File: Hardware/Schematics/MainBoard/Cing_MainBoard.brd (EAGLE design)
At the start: 100 x 100 mm, 174 parts, among them IC1 L293D, IC2 LM2576S, IC3 FT232RL, IC5 BME280, Q1 16mhz, Q2 BSS138, Q3 BSS138, Q4 BSS138, Q5 BSS138, Q6 NP2301AMR-G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

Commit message: 3D package upgrade
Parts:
- VERSION: value 3.1 -> 4.0
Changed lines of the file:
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@@
 </layers>
 <board>
-<fusionsync huburn="a.cGVyc29uYWw6dWUyOTc5YzVj" projecturn="a.cGVyc29uYWw6dWUyOTc5YzVjIzIwMTYxMDE1NDY4MTE5MjY" f3durn="urn:adsk.wipprod:dm.lineage:OxtLfXioRNGpEPjqi8H5ew" pcbguid="aab246c0-a25e-424b-8ec7-c8b2cc11dcb0" lastpulledtime="" lastsyncedchangeguid="ba3a4b8f-c2b4-ea65-9e96-2cd773722963"/>
+<fusionsync huburn="a.cGVyc29uYWw6dWUyOTc5YzVj" projecturn="a.cGVyc29uYWw6dWUyOTc5YzVjIzIwMTkwNjI1MjAwNjYyNTAx" f3durn="urn:adsk.wipprod:dm.lineage:F-kKAJn1SLWSqLFyv44BXQ" pcbguid="94010e1c-0bc5-45e6-b30e-e8625a835ba8" lastpulledtime="" lastsyncedchangeguid="c102dd65-50ae-9bd8-6df9-751ffc4031cd"/>
 <plain>
 <text x="17.145" y="28.448" size="1.778" layer="21">Header 2</text>
@@
 <attribute name="VALUE" x="39.5" y="39.5" size="1.27" layer="21" rot="R135" align="bottom-center"/>
 </element>
-<element name="U$20" library="Cing Library" library_urn="urn:adsk.eagle:library:10154637" package="BALL" package3d_urn="urn:adsk.eagle:package:10154728/1" override_package3d_urn="urn:adsk.eagle:package:11838365/3" override_package_urn="urn:adsk.eagle:footprint:10154687/1" value="BALL" x="45" y="0" smashed="yes"/>
+<element name="U$20" library="Cing Library" library_urn="urn:adsk.eagle:library:10154637" package="BALL" package3d_urn="urn:adsk.eagle:package:10154728/1" override_package3d_urn="urn:adsk.eagle:package:11838365/5" override_package_urn="urn:adsk.eagle:footprint:10154687/1" value="BALL" x="45" y="0" smashed="yes"/>
 <element name="LED5" library="Cing Library" library_urn="urn:adsk.eagle:library:10154637" package="WS2812B" package3d_urn="urn:adsk.eagle:package:10154742/1" override_package3d_urn="urn:adsk.eagle:package:11838153/2" override_package_urn="urn:adsk.eagle:footprint:10154705/1" value="WS2812B" x="-34.29" y="-34.29" smashed="yes" rot="R270"/>
 <element name="LED6" library="Cing Library" library_urn="urn:adsk.eagle:library:10154637" package="WS2812B" package3d_urn="urn:adsk.eagle:package:10154742/1" override_package3d_urn="urn:adsk.eagle:package:11838143/2" override_package_urn="urn:adsk.eagle:footprint:10154705/1" value="WS2812B" x="-34.29" y="34.29" smashed="yes" rot="R180"/>
@@
 <attribute name="NAME" x="15.813" y="-26.546" size="1.27" layer="21" rot="R90"/>
 </element>
-<element name="VERSION" library="Cing Library" library_urn="urn:adsk.eagle:library:10154637" package="VERSION" package3d_urn="urn:adsk.eagle:package:10154717/1" value="3.1" x="49.5" y="0" smashed="yes" rot="R90">
+<element name="VERSION" library="Cing Library" library_urn="urn:adsk.eagle:library:10154637" package="VERSION" package3d_urn="urn:adsk.eagle:package:10154717/1" value="4.0" x="49.5" y="0" smashed="yes" rot="R90">
 <attribute name="VALUE" x="46.5" y="6.84" size="2.54" layer="21" rot="R90" align="center"/>
 </element>
@@
 <attribute name="VALUE" x="3.942" y="-33.6" size="1.27" layer="28" rot="MR90"/>
 </element>
-<element name="U$15" library="diy-modules" package="COMPASS-HMC5883L" override_package3d_urn="urn:adsk.eagle:package:11838453/4" override_package_urn="urn:adsk.eagle:footprint:11838454/1" value="" x="24.2" y="40.3" smashed="yes" rot="MR90">
+<element name="U$15" library="diy-modules" package="COMPASS-HMC5883L" override_package3d_urn="urn:adsk.eagle:package:11838453/5" override_package_urn="urn:adsk.eagle:footprint:11838454/1" value="" x="24.2" y="40.3" smashed="yes" rot="MR90">
 <attribute name="VALUE" x="16.58" y="40.3" size="1.27" layer="28" rot="MR90" align="top-center"/>
 </element>

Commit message: commit
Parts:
- added C23: 47uf, rcl:153CLV-0505
- added C24: 100n, rcl:C1206
- C17: value (none) -> 47uf; device rcl:E3,5-8 -> rcl:153CLV-0505
- moved C17 6.52 mm to (-20.9, 30.0), turned to 270 degrees
- moved R3 0.30 mm to (-23.1, -29.5)
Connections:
- net GND: now also C23.-, C24.2
- net VCC_MOT: now also C23.+, C24.1
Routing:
- net GND: track 832.2 -> 849.9 mm
- net VCC_MOT: track 42.9 -> 54.6 mm
- net VCC_SERVO: track 415.3 -> 421.4 mm, vias 11 -> 12
- net MOT_A+: track 71.5 -> 73.0 mm
- net BAT+: track 315.7 -> 314.4 mm
- net N$1: track 100.0 -> 98.8 mm
- net N$44: track 35.0 -> 34.0 mm
- net ATMEGA_D-: track 107.7 -> 106.6 mm
- net N$8: track 22.6 -> 21.6 mm

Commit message: commit
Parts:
- added C25, C26: 100n, rcl:C1206
- IC1: value L293D -> L293D
- moved C13 1.98 mm to (38.3, 31.8), turned to 90 degrees
- moved SW1 1.60 mm to (-43.8, -32.7)
- moved C9 1.08 mm to (-40.5, 35.2)
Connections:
- net +3V3: now also C26.2; no longer LED10.2, LED11.2, LED4.2, LED5.1, LED6.1, LED7.1, LED8.1, LED9.2
- net BAT+: no longer U$23.5
- net BUTTON: now also C26.1
- net GND: now also C25.1
- net RESET: now also C25.2
- net VCC_SERVO: now also LED10.2, LED11.2, LED4.2, LED5.1, LED6.1, LED7.1, LED8.1, LED9.2, U$23.5
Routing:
- net VCC_SERVO: track 421.4 -> 521.4 mm, vias 12 -> 15
- net GND: track 849.9 -> 874.9 mm, vias 45 -> 46
- net +3V3: track 661.1 -> 644.9 mm, vias 39 -> 40
- net RESET: track 195.4 -> 209.7 mm
- net BUTTON: track 19.0 -> 24.0 mm
- net N$1: track 98.8 -> 95.3 mm
- net SDA: track 247.9 -> 245.0 mm
- net ATMEGA_D+: track 102.2 -> 105.0 mm
- net D-: track 25.7 -> 23.3 mm
- net N$24: track 15.6 -> 13.3 mm
- net BAT-: track 106.4 -> 108.7 mm
- net D+: track 21.7 -> 19.4 mm
- net MOT_B-: track 66.5 -> 64.4 mm
- net N$13: track 18.2 -> 16.1 mm
- net SCL: track 241.2 -> 239.5 mm
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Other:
- board text added: "I2C"
- board text added: "USB"
- board text removed: "BT"

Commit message: commit
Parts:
- added U$10: MT3608SOT23-6, MT3608:SOT23-6
- moved R46 3.05 mm to (-13.0, 20.2), turned to 90 degrees
- moved R9 1.39 mm to (-15.2, 20.2), turned to 270 degrees
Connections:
- removed net N$44: D3.A, L1.2, U$5.P$1
- new net N$67: D3.A, L1.2, U$10.P$1, U$5.P$1
- net BAT+: now also U$10.P$4, U$10.P$5
- net GND: now also U$10.P$2
- net N$35: now also U$10.P$3
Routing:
- net N$67: track 0.00 -> 48.6 mm, vias 0 -> 2
- net N$44: track 34.0 -> 0.00 mm
- net N$46: track 33.7 -> 38.9 mm
- net N$35: track 15.5 -> 20.3 mm
- net BAT+: track 315.6 -> 319.6 mm
- net GND: track 874.9 -> 877.3 mm

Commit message: commit
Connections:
- net +3V3: no longer IC1.16
- net VCC_SERVO: now also IC1.16
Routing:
- net VCC_SERVO: track 521.4 -> 591.6 mm, vias 15 -> 18
- net +3V3: track 644.9 -> 634.0 mm, vias 40 -> 41
- net SDA: track 245.0 -> 246.1 mm
- net IN_A1: track 92.3 -> 91.6 mm
- net IN_B2: track 42.5 -> 41.8 mm

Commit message: commit
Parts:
- removed U$10: MT3608SOT23-6, MT3608:SOT23-6
- moved R46 3.05 mm to (-14.2, 17.4), turned to 45 degrees
- moved R9 1.39 mm to (-15.7, 18.9), turned to 225 degrees
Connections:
- removed net N$67: D3.A, L1.2, U$10.P$1, U$5.P$1
- new net N$44: D3.A, L1.2, U$5.P$1
- net +3V3: now also IC1.16
- net BAT+: no longer U$10.P$4, U$10.P$5
- net GND: no longer U$10.P$2
- net N$35: no longer U$10.P$3
- net VCC_SERVO: no longer IC1.16
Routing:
- net VCC_SERVO: track 591.6 -> 521.4 mm, vias 18 -> 15
- net N$67: track 48.6 -> 0.00 mm, vias 2 -> 0
- net N$44: track 0.00 -> 34.0 mm
- net +3V3: track 634.0 -> 644.9 mm, vias 41 -> 40
- net N$46: track 38.9 -> 33.7 mm
- net N$35: track 20.3 -> 15.5 mm
- net BAT+: track 319.6 -> 315.6 mm
- net GND: track 877.3 -> 874.9 mm
- net SDA: track 246.1 -> 245.0 mm
- net IN_A1: track 91.6 -> 92.3 mm
- net IN_B2: track 41.8 -> 42.5 mm

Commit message: commit
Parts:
- removed IRFU9024: IRFU9024, Cing Library:IRFU9024
- added C27: 10uf, rcl:153CLV-0505
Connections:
- net BAT-: now also C27.-, Q6.1, Q7.1
- net GND: no longer IRFU9024.G, Q6.1, Q7.1
- net IRFU: no longer IRFU9024.D
- net N$26: now also C27.+; no longer IRFU9024.S
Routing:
- net BAT-: track 108.7 -> 131.5 mm, vias 2 -> 4
- net GND: track 874.9 -> 865.5 mm
- net N$26: track 29.3 -> 35.6 mm, vias 2 -> 3
- net IRFU: track 81.0 -> 77.0 mm, vias 2 -> 3

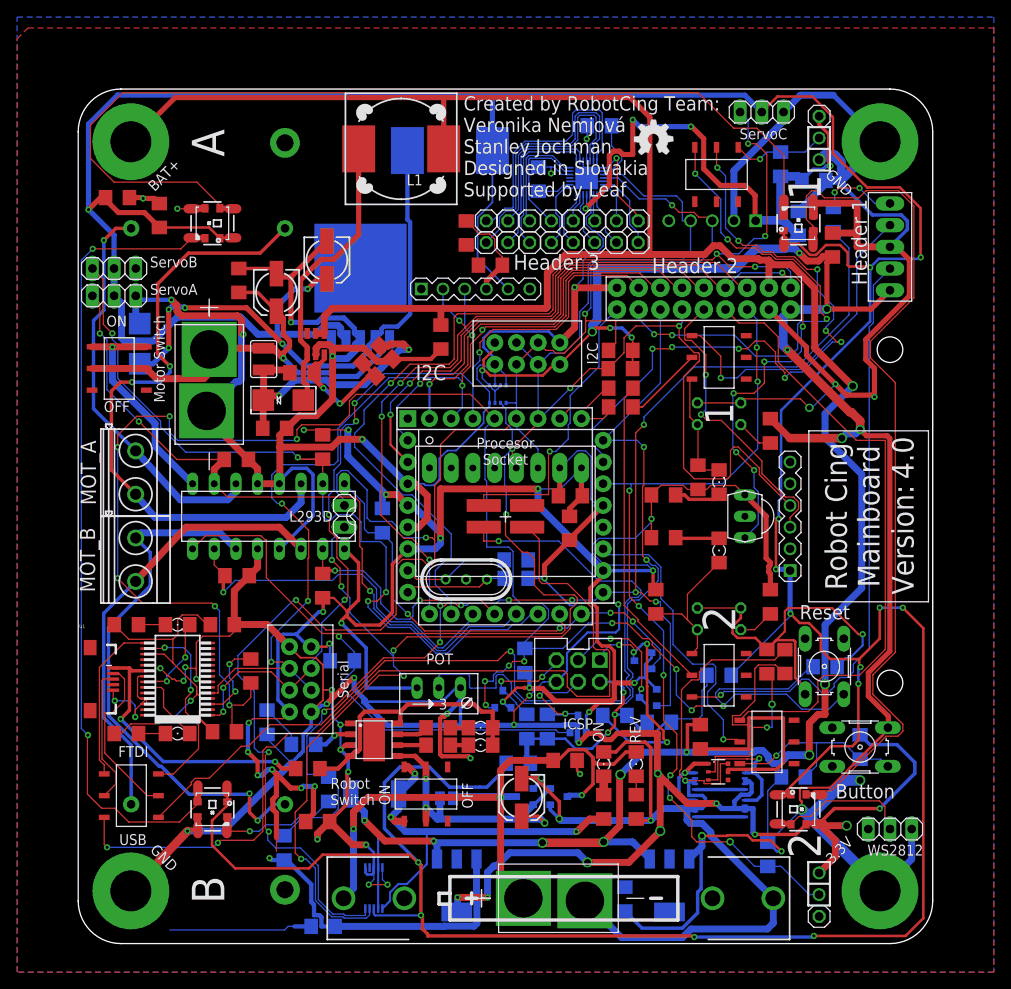
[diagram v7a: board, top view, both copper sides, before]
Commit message: adding more protection (motor fix)
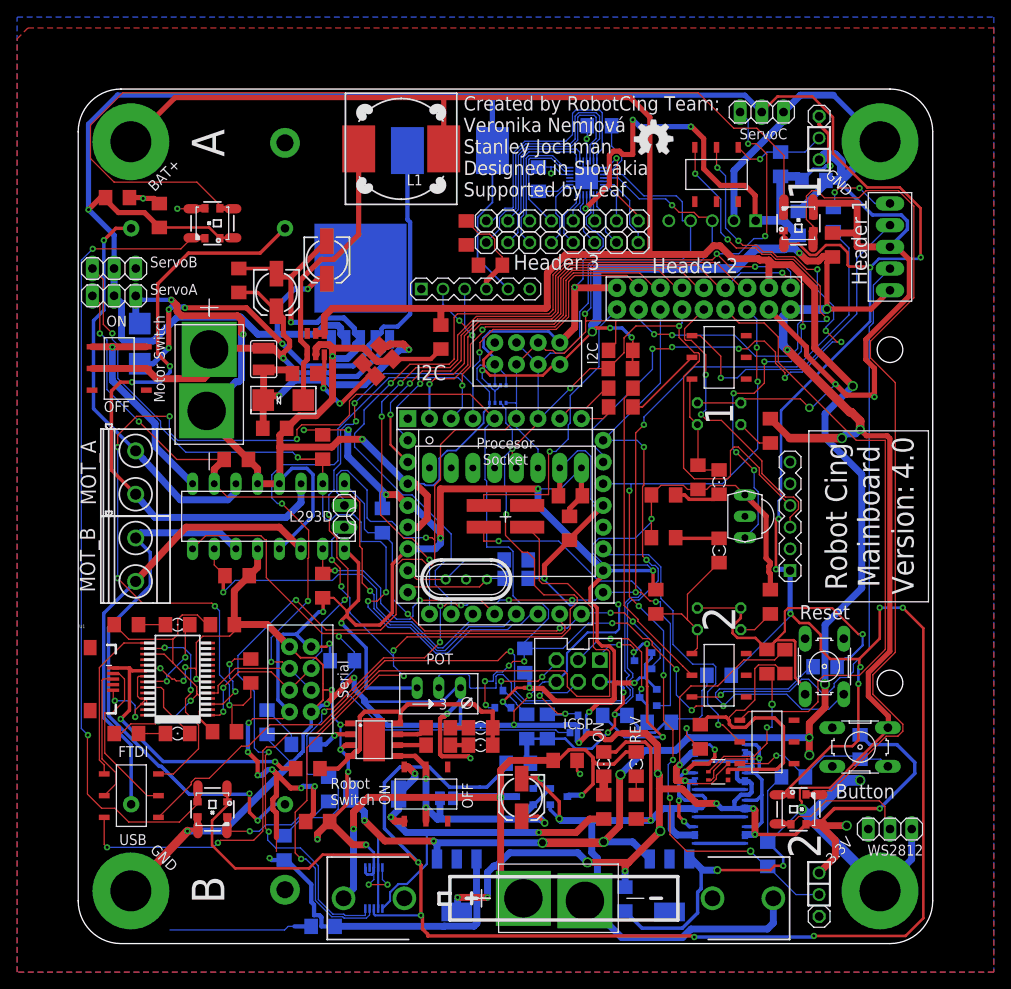
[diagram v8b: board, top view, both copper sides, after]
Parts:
- added T1, T2: FS8205, FS8205A:TSSOP-8
- 1, 8205: value 8205 -> FS8205
- moved R49 0.32 mm to (-23.5, 16.7)
- turned R48 to 270 degrees
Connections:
- new net N$67: T1.1, T1.8
- new net N$68: T2.1, T2.8
- net BAT-: now also T1.2, T1.3, T2.2, T2.3
- net GND: now also T1.6, T1.7, T2.6, T2.7
- net N$48: now also T1.4, T2.4
- net N$49: now also T1.5, T2.5
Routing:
- net N$48: track 9.40 -> 18.9 mm, vias 1 -> 4
- net GND: track 865.5 -> 874.9 mm, vias 46 -> 48
- net N$49: track 16.7 -> 24.2 mm
- net N$68: track 0.00 -> 5.85 mm
- net N$67: track 0.00 -> 5.85 mm
- net N$50: track 40.0 -> 35.0 mm
- net BAT+: track 315.6 -> 310.7 mm, vias 9 -> 10
- net BUTTON: track 24.0 -> 20.4 mm
- net +3V3: track 644.9 -> 642.1 mm
- net BAT-: track 131.5 -> 133.4 mm, vias 4 -> 5
- net N$54: track 19.5 -> 17.6 mm
- net MISO_HV: track 30.1 -> 28.5 mm
- net A7: track 99.5 -> 100.5 mm
- net N$35: track 15.5 -> 16.4 mm
- net A6: track 35.1 -> 34.4 mm
